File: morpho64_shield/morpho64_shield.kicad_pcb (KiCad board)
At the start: 2 copper layers, 70 x 57 mm, 6 parts, among them J1 CN7, J2 CN10

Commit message: Update morpho64_shield.kicad_pcb
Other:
- board text added: "USER▶"
- board text added: "◀RESET"
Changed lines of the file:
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@@
 		)
+	)
+	(gr_line
+		(start 124.5235 59.6265)
+		(end 124.5235 108.0135)
+		(stroke
+			(width 0.12)
+			(type solid)
+		)
+		(layer "F.SilkS")
+	)
+	(gr_line
+		(start 180.2765 59.6265)
+		(end 185.4835 59.6265)
+		(stroke
+			(width 0.12)
+			(type solid)
+		)
+		(layer "F.SilkS")
+	)
+	(gr_line
+		(start 119.3165 108.0135)
+		(end 119.3165 59.6265)
+		(stroke
+			(width 0.12)
+			(type solid)
+		)
+		(layer "F.SilkS")
+	)
+	(gr_line
+		(start 119.3165 59.6265)
+		(end 124.5235 59.6265)
+		(stroke
+			(width 0.12)
+			(type solid)
+		)
+		(layer "F.SilkS")
+	)
+	(gr_line
+		(start 185.4835 59.6265)
+		(end 185.4835 108.0135)
+		(stroke
+			(width 0.12)
+			(type solid)
+		)
+		(layer "F.SilkS")
+	)
+	(gr_line
+		(start 180.2765 108.0135)
+		(end 180.2765 59.6265)
+		(stroke
+			(width 0.12)
+			(type solid)
+		)
+		(layer "F.SilkS")
+	)
+	(gr_line
+		(start 185.4835 108.0135)
+		(end 180.2765 108.0135)
+		(stroke
+			(width 0.12)
+			(type solid)
+		)
+		(layer "F.SilkS")
+	)
+	(gr_line
+		(start 124.5235 108.0135)
+		(end 119.3165 108.0135)
+		(stroke
+			(width 0.12)
+			(type solid)
+		)
+		(layer "F.SilkS")
 	)
 	(gr_arc
@@
 		)
 		(layer "Edge.Cuts")
+	)
+	(gr_text "◀RESET"
+		(at 167.64 58.42 0)
+		(layer "F.SilkS" knockout)
+		(effects
+			(font
+				(size 1.016 1.016)
+				(thickness 0.254)
+				(bold yes)
+			)
+			(justify left)
+		)
+	)
+	(gr_text "USER▶"
+		(at 137.16 58.42 0)
+		(layer "F.SilkS" knockout)
+		(effects
+			(font
+				(size 1.016 1.016)
+				(thickness 0.254)
+				(bold yes)
+			)
+			(justify right)
+		)
 	)
 	(zone
@@
 		)
 	)
-	(group ""
-		(members "0d140630-bca3-49aa-b87d-8d6170f14bc6" "1e40f413-7ec0-40a5-8839-53505a2c6e0a"
-			"2275657d-a53d-488c-9030-e2f2dabe9318" "233bb4ba-a8d2-4a75-9ed1-4a6f4ff595d1"
-			"33f5d391-c550-4f76-a0c5-83bcefefd0cf" "446f670b-42c1-4bbe-904a-5b88769e6943"
-			"4dd7b11a-2cef-4a32-821a-791dfac6bed1" "ab0bcea5-bf33-4ac2-b115-6a630fbaf967"
-			"c29b4a8b-e744-44f5-a5fa-d08552dcebf7" "db37066f-6a8c-46f3-8757-d11ea7477588"
-			"dd624fa4-2d13-407e-ab04-5fbf28366655" "ddf92cb8-00df-4670-8835-9b206669a0af"
-			"e13b6391-877d-4a18-90dc-52d97e51df89" "f220bd89-d1c8-43ff-b935-35ef54671148"
-		)
-	)

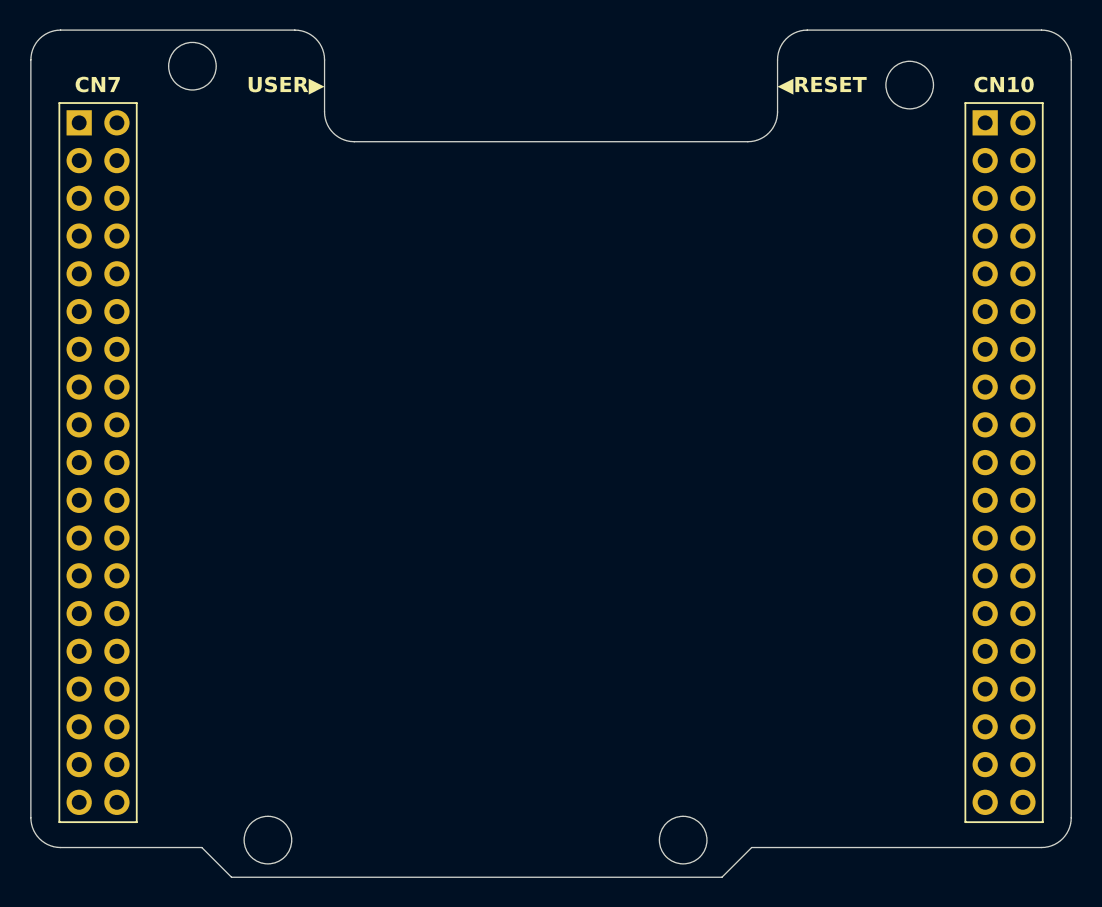
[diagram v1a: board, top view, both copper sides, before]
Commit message: added silkscreen labels
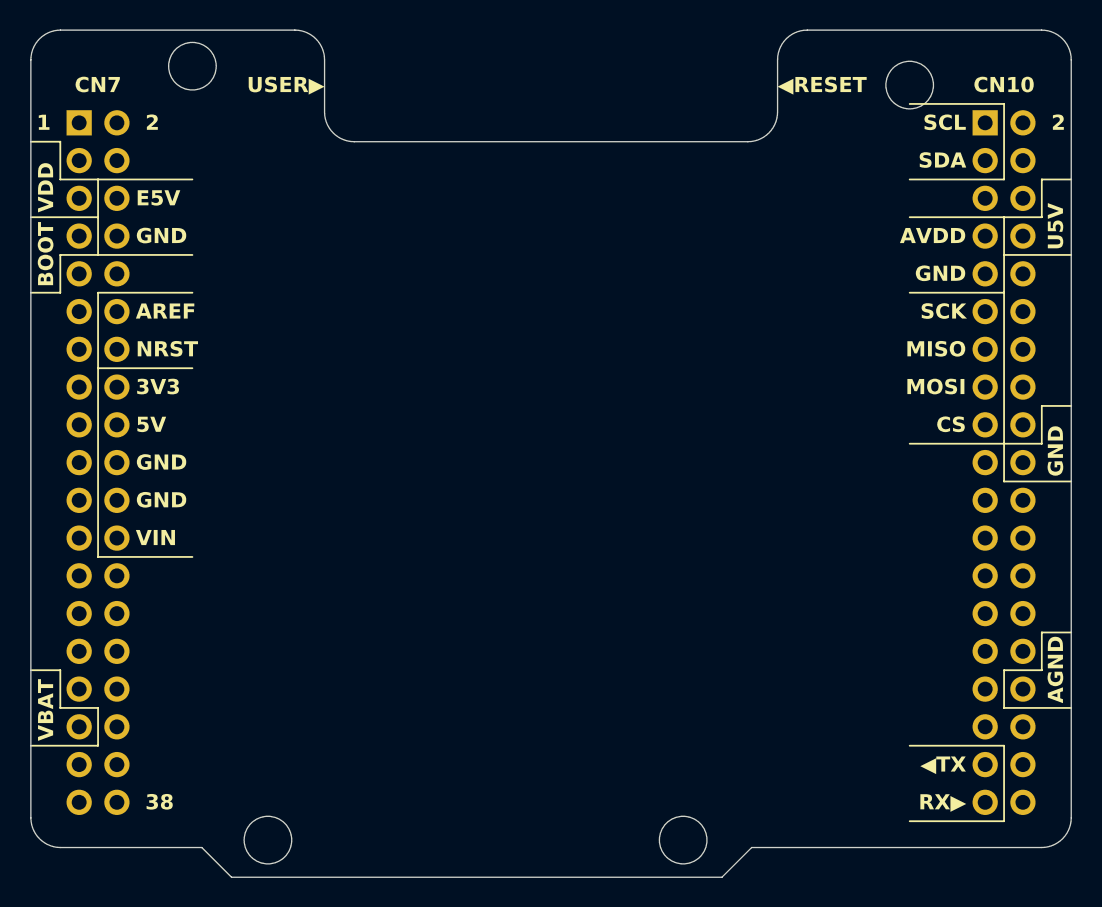
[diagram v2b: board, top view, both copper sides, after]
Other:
- board text added: "1"
- board text added: "2"
- board text added: "38"
- board text added: "3V3"
- board text added: "5V"
- board text added: "AGND"
- board text added: "AREF"
- board text added: "AVDD"
- board text added: "BOOT"
- board text added: "CS"
- board text added: "E5V"
- board text added: "GND"
- board text added: "MISO"
- board text added: "MOSI"
- board text added: "NRST"
- board text added: "RX▶"
- board text added: "SCK"
- board text added: "SCL"
- board text added: "SDA"
- board text added: "U5V"
- board text added: "VBAT"
- board text added: "VDD"
- board text added: "VIN"
- board text added: "◀TX"
